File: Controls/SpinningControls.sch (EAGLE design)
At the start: 21 parts, among them IC1 S-19246E33H-V5T2U, J1 SULLINS_PPPC062LFBN-RCSULLINS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, J10 SULLINS_PPPC062LFBN-RCSULLINS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, J11 SULLINS_PPPC062LFBN-RCSULLINS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, J2 7-146256-0, J3 F32R-1A7H1-11040, J4 SULLINS_PPPC062LFBN-RCSULLINS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, J5 SULLINS_PPPC062LFBN-RCSULLINS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, J6 SULLINS_PPPC062LFBN-RCSULLINS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, J7 SULLINS_PPPC062LFBN-RCSULLINS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, J8 SULLINS_PPPC062LFBN-RCSULLINS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, J9 SULLINS_PPPC062LFBN-RCSULLINS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, X1 22-23-2021

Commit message: controls layout partial
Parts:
- removed TP1: RCWCTE, RCWCTE:RCWCTE
- removed X1: 22-23-2021, con-molex:22-23-2021
- added FPGA: DE0-NANO, VoxelEagleLib:DE0-NANO
- added IC2, IC3, IC4: SN74LVC1G34DBVR, SN74LVC1G34DBVR:SN74LVC1G34DBVR
- added J12, J13, J14: SULLINS_PPPC062LFBN-RCSULLINS_PPPC062LFBN-RC_0_0, Sullins - PPPC062LFBN-RC:SULLINS_PPPC062LFBN-RCSULLINS_PPPC062LFBN-RC_0_0
- added J15: 430450612, molex:430450612
- added J16, J17: 430450412, molex:430450412
- added J18, J19: 436500215, molex:436500215
- added R1, R2: 165 Ω, rcl:R-US_R0603
- added R3, R5: 19.1k Ω, rcl:R-US_R0402
- J1: value SULLINS_PPPC062LFBN-RCSULLINS_PPPC062LFBN-RC_0_0 -> 7-146256-0; device Sullins - PPPC062LFBN-RC:SULLINS_PPPC062LFBN-RCSULLINS_PPPC062LFBN-RC_0_0 -> SamacSys_Parts:7-146256-0
- J2: value 7-146256-0 -> F32R-1A7H1-11040; device SamacSys_Parts:7-146256-0 -> F32R-1A7H1-11040:F32R-1A7H1-11040
- J3: value F32R-1A7H1-11040 -> SULLINS_PPPC062LFBN-RCSULLINS_PPPC062LFBN-RC_0_0; device F32R-1A7H1-11040:F32R-1A7H1-11040 -> Sullins - PPPC062LFBN-RC:SULLINS_PPPC062LFBN-RCSULLINS_PPPC062LFBN-RC_0_0
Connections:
- net 3V3_DRV renamed 3V3_LOGIC
- removed net N$8: C3.2, IC1.VSS
- new net ACTIVE: J1.31, J2.31
- new net B1: J1.21, J2.21
- new net B2: J1.22, J2.22
- new net B3: J1.23, J2.23
- new net B4: J1.24, J2.24
- new net B5: J1.25, J2.25
- new net B6: J1.26, J2.26
- new net B7: J1.27, J2.27
- new net B8: J1.28, J2.28
- new net DISPEN: J1.34, J2.34
- new net ENC_POS: J15.4, R2.2
- new net ENC_POS0: R1.2
- new net G1: J1.13, J2.13
- new net G2: J1.14, J2.14
- new net G3: J1.15, J2.15
- new net G4: J1.16, J2.16
- new net G5: J1.17, J2.17
- new net G6: J1.18, J2.18
- new net G7: J1.19, J2.19
- new net G8: J1.20, J2.20
- new net GSCLK: IC4.Y
- new net GSCLK_FPGA: IC4.A
- new net HSYNC: J1.32, J2.32
- new net LAT: IC2.Y
- new net LAT_FPGA: IC2.A
- new net N$10: FPGA.GND4
- new net N$11: FPGA.VCC_SYS_1
- new net N$12: FPGA.VCC3P3_1
- new net N$13: FPGA.GND1
- new net N$14: FPGA.GND2
- new net N$15: FPGA.ANALOG_IN5
- new net N$16: FPGA.ANALOG_IN7
- new net N$17: FPGA.ANALOG_IN2
- new net N$18: FPGA.ANALOG_IN0
- new net N$19: FPGA.ANALOG_IN6
- new net N$20: FPGA.ANALOG_IN3
- new net N$21: FPGA.ANALOG_IN4
- new net N$22: FPGA.ANALOG_IN1
- new net N$23: FPGA.VCC3P3_3
- new net N$24: FPGA.GND5
- new net N$3: FPGA.VCC_SYS_2
- new net N$7: FPGA.GND3
- new net N$9: FPGA.VCC3P3_2
- new net PIXCLK: J1.30, J2.30
- new net PI_RX: J15.5, U$1.RXD0/GPIO15
- new net PI_TX: J15.6, U$1.TXD0/GPIO14
- new net R1: J1.5, J2.5
- new net R2: J1.6, J2.6
- new net R3: J1.7, J2.7
- new net R4: J1.8, J2.8
- new net R5: J1.9, J2.9
- new net R6: J1.10, J2.10
- new net R7: J1.11, J2.11
- new net R8: J1.12, J2.12
- new net SCLK: IC3.Y
- new net SCLK_FPGA: IC3.A
- new net VSYNC: J1.33, J2.33
- net 24V: now also J15.2, U$3.VIN, U$6.VIN; no longer X1-1.S
- net 5V: now also IC2.VCC, IC3.VCC, IC4.VCC, J16.3, J17.3, J18.2, J19.2, R3.2, R5.2, U$1.5V0@1, U$1.5V0@2
- net GND: now also C3.2, IC1.VSS, IC2.GND, IC3.GND, IC4.GND, J15.1, J16.1, J17.1, J18.1, J19.1, U$1.GND@8, U$3.GND, U$6.GND; no longer X1-2.S
- net N$1: now also J16.4, R5.1; no longer U$3.VIN
- net N$2: now also J17.4, R3.1; no longer U$3.GND
- net N$5: now also J16.2, R1.1; no longer U$6.VIN
- net N$6: now also J17.2, R2.1; no longer U$6.GND
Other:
- note added: "FPGA Power"
- moved on the sheet: C1, C2, C3, IC1, U$1, U$6

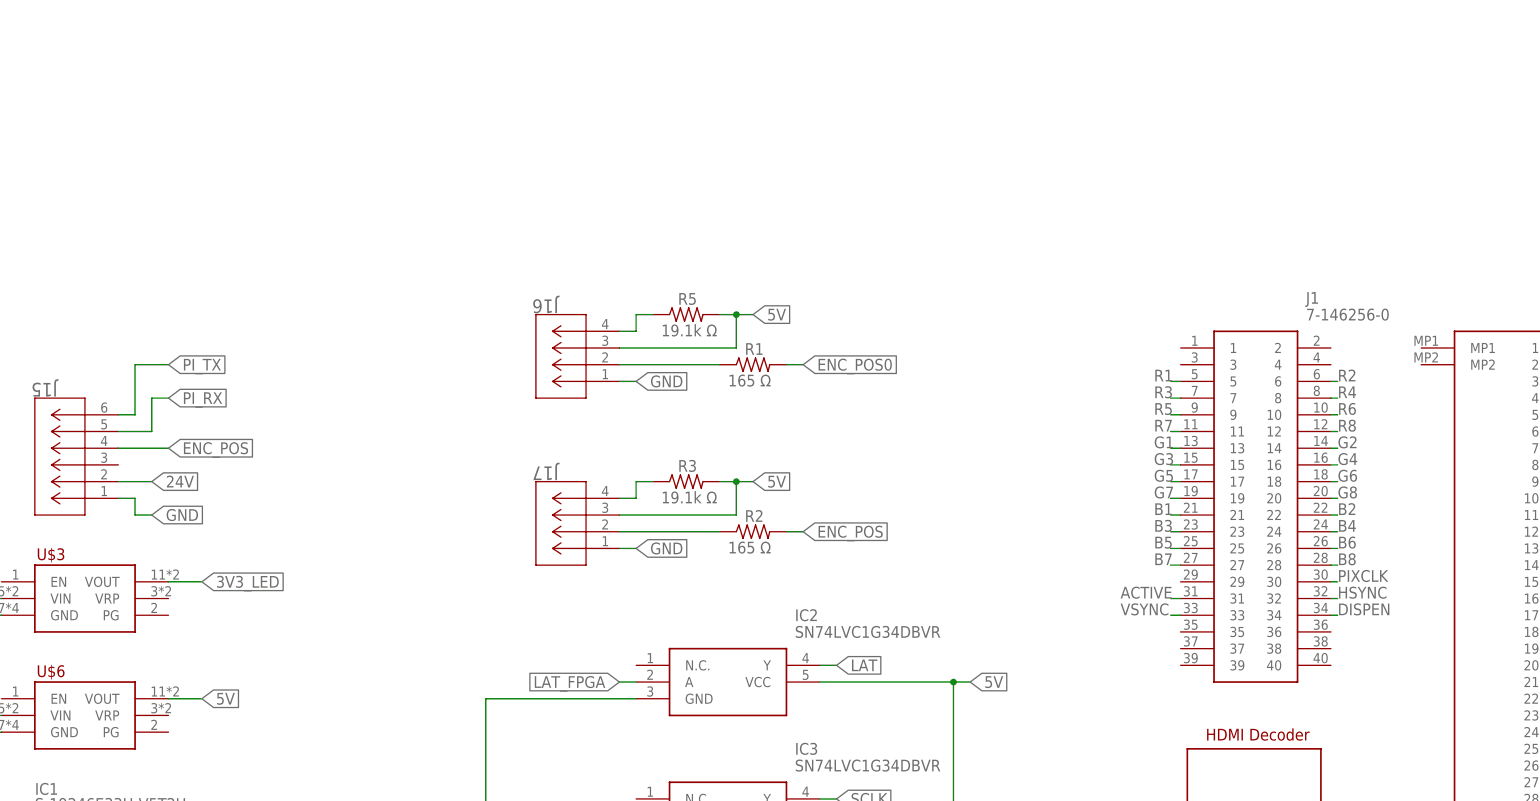
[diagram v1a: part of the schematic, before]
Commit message: parts exchange, layout corrections, no routing
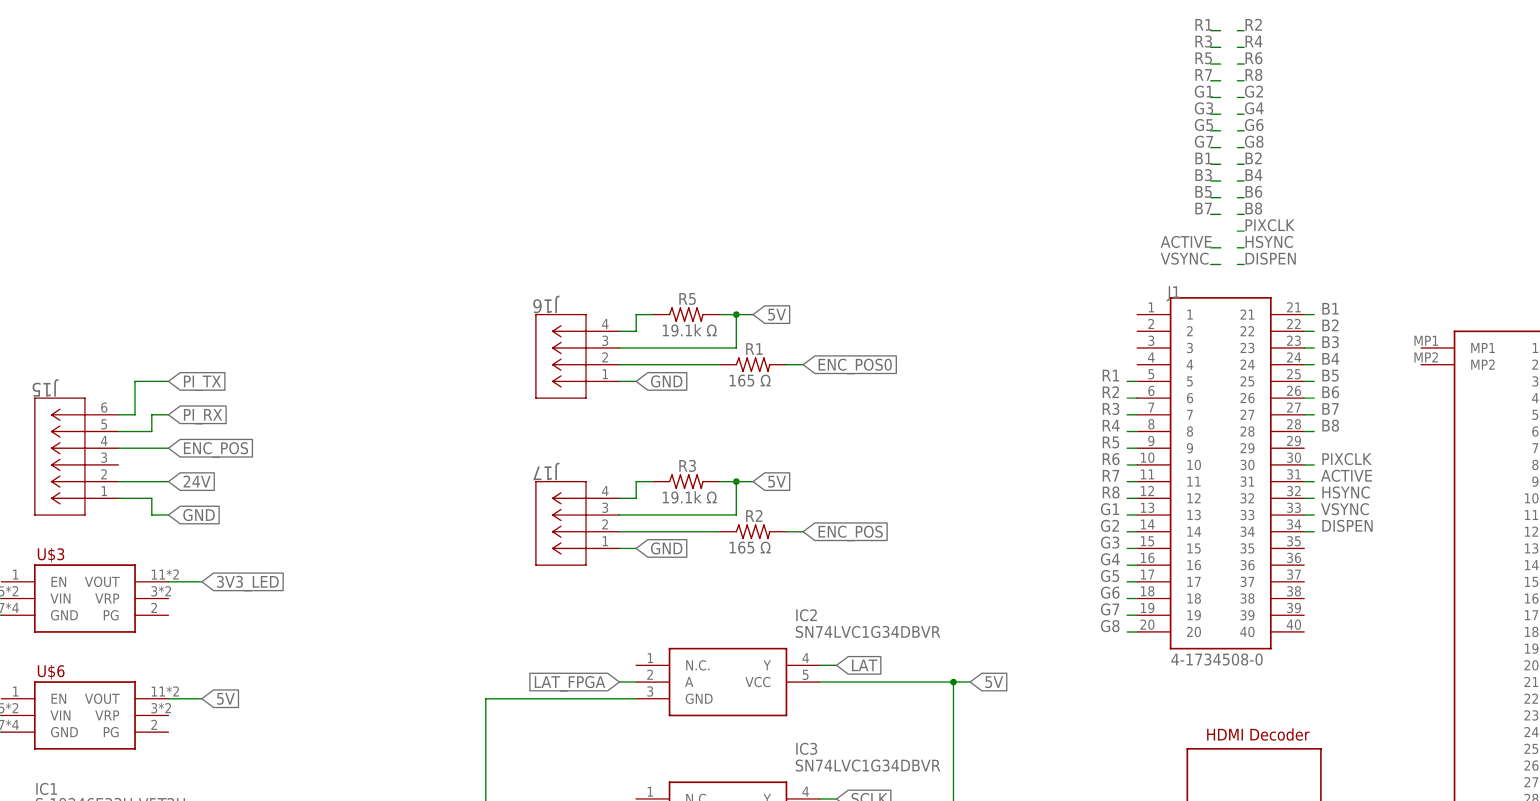
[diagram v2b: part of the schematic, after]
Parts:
- J1: value 7-146256-0 -> 4-1734508-0; device SamacSys_Parts:7-146256-0 -> 4-1734508-0:4-1734508-0
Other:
- moved on the sheet: J1

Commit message: Fixed encoder on spinning controls board
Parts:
- removed J1: 4-1734508-0, 4-1734508-0:4-1734508-0
- removed R5: 19.1k Ω, rcl:R-US_R0402
- added C10, C11, C12, C13, C14, C15, C4, C5, C6, C7, C8, C9: 100u, GTOR - Passive Components:CAP_THTE2-5
- added R4: 19.1k Ω, rcl:R-US_R0402
- J16, J17: value 430450412 -> 430450612; device molex:430450412 -> molex:430450612
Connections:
- removed net N$2: J17.4, R3.1
- removed net N$5: J16.2, R1.1
- net 3V3_LED: now also C10.+, C11.+, C12.+, C13.+, C14.+, C15.+, C4.+, C5.+, C6.+, C7.+, C8.+, C9.+
- net 3V3_LOGIC: now also IC2.VCC, IC3.VCC, IC4.VCC
- net 5V: now also R1.2, R2.2; no longer IC2.VCC, IC3.VCC, IC4.VCC, R3.2, R5.2
- net ACTIVE: no longer J1.31
- net B1: no longer J1.21
- net B2: no longer J1.22
- net B3: no longer J1.23
- net B4: no longer J1.24
- net B5: no longer J1.25
- net B6: no longer J1.26
- net B7: no longer J1.27
- net B8: no longer J1.28
- net DISPEN: no longer J1.34
- net ENC_POS: now also J17.4, R3.1; no longer R2.2
- net ENC_POS0: now also J16.4, R4.1; no longer R1.2
- net G1: no longer J1.13
- net G2: no longer J1.14
- net G3: no longer J1.15
- net G4: no longer J1.16
- net G5: no longer J1.17
- net G6: no longer J1.18
- net G7: no longer J1.19
- net G8: no longer J1.20
- net GND: now also C10.-, C11.-, C12.-, C13.-, C14.-, C15.-, C4.-, C5.-, C6.-, C7.-, C8.-, C9.-, J15.3, J16.2, J16.5, J17.2, J17.5, R3.2, R4.2; no longer J16.1, J17.1
- net HSYNC: no longer J1.32
- net N$1: now also J16.1, R1.1; no longer J16.4, R5.1
- net N$6: now also J17.1; no longer J17.2
- net PIXCLK: no longer J1.30
- net R1: no longer J1.5
- net R2: no longer J1.6
- net R3: no longer J1.7
- net R4: no longer J1.8
- net R5: no longer J1.9
- net R6: no longer J1.10
- net R7: no longer J1.11
- net R8: no longer J1.12
- net VSYNC: no longer J1.33
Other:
- note added: "GREEN BLUE WHITE BLACK RED"
- moved on the sheet: R3
